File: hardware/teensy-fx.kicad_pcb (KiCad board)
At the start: 2 copper layers, 60 x 105 mm, 62 parts, among them J1 AudioJack3_Ground, J2 AudioJack3_Ground, SW1 Switch_SW_Push, SW2 Switch_SW_Push, SW3 Switch_SW_Push, SW4 Switch_SW_Push, U1 Teensy4.0, U2 AP7313-1.8V, U3 SGTL5000, U4 4067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

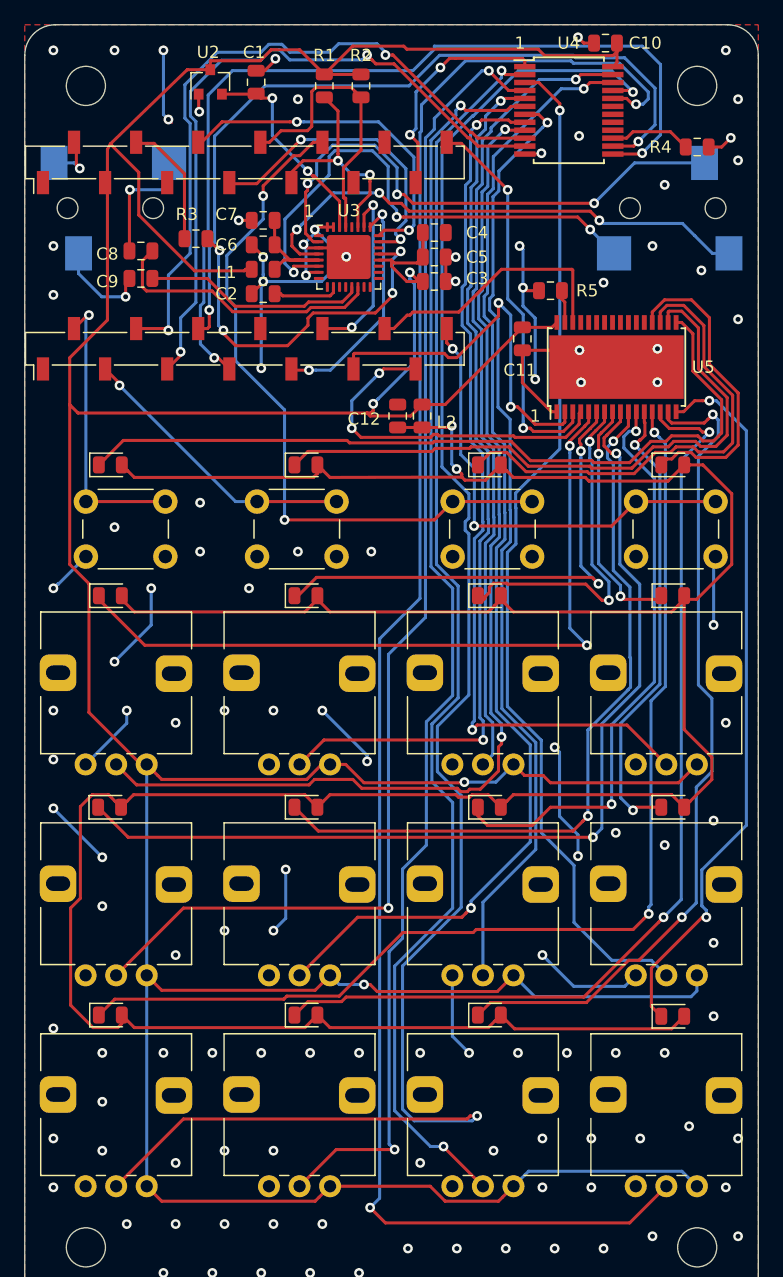
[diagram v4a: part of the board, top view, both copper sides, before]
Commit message: try to fix the wiring a bit, signal integrity might be an issue with 2 layer and teensy breakout
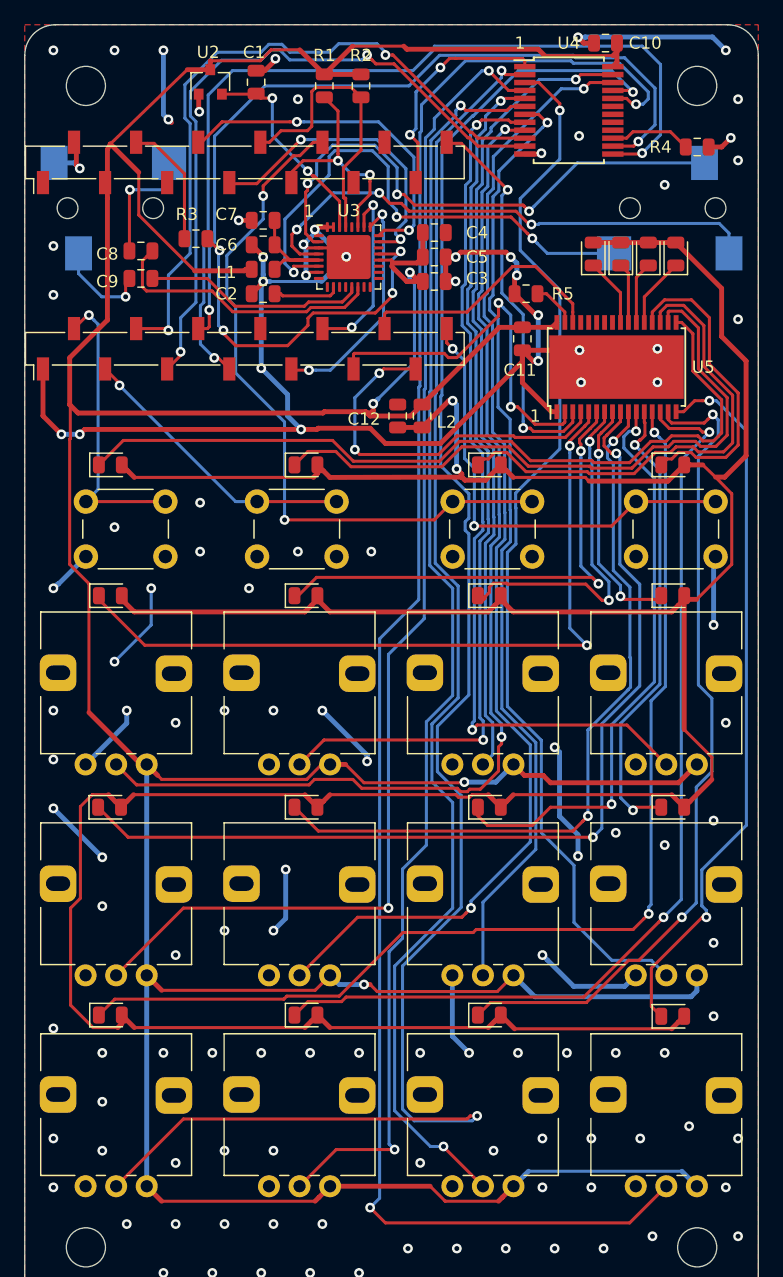
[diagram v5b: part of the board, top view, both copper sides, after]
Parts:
- added D17: LED, LED_SMD:LED_0805_2012Metric, F.Cu at (278.2, 63.8)
- added D18: LED, LED_SMD:LED_0805_2012Metric, F.Cu at (276.0, 63.8)
- added D19: LED, LED_SMD:LED_0805_2012Metric, F.Cu at (273.8, 63.8)
- added D20: LED, LED_SMD:LED_0805_2012Metric, F.Cu at (271.5, 63.8)
- moved R5 2.02 mm to (266.0, 67.0)
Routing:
- net GND: track 147.7 -> 218.1 mm, vias 122 -> 123
- net +3.3VA: track 265.4 -> 298.2 mm
- net Net-(D17-Pad1): track 0.00 -> 5.73 mm
- net Net-(D20-Pad1): track 0.00 -> 5.58 mm
- net Net-(D18-Pad1): track 0.00 -> 5.07 mm
- net Net-(D19-Pad1): track 0.00 -> 4.92 mm
- net /pots buttons & LEDs/a6: track 83.9 -> 86.6 mm
- net led_data: track 29.2 -> 30.9 mm
- net Net-(D13-Pad1): track 64.8 -> 66.1 mm
- net Net-(D14-Pad1): track 51.9 -> 52.9 mm
- net Net-(J2-PadS): track 42.6 -> 43.7 mm
- net led_latch: track 21.7 -> 21.0 mm
- net sw_1: track 23.5 -> 24.2 mm
- net Net-(R5-Pad1): track 3.15 -> 3.71 mm
- net Net-(J2-PadR): track 44.6 -> 45.2 mm
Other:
- net class power added: clearance 0.2, trace_width 0.4, via_dia 0.8, via_drill 0.4

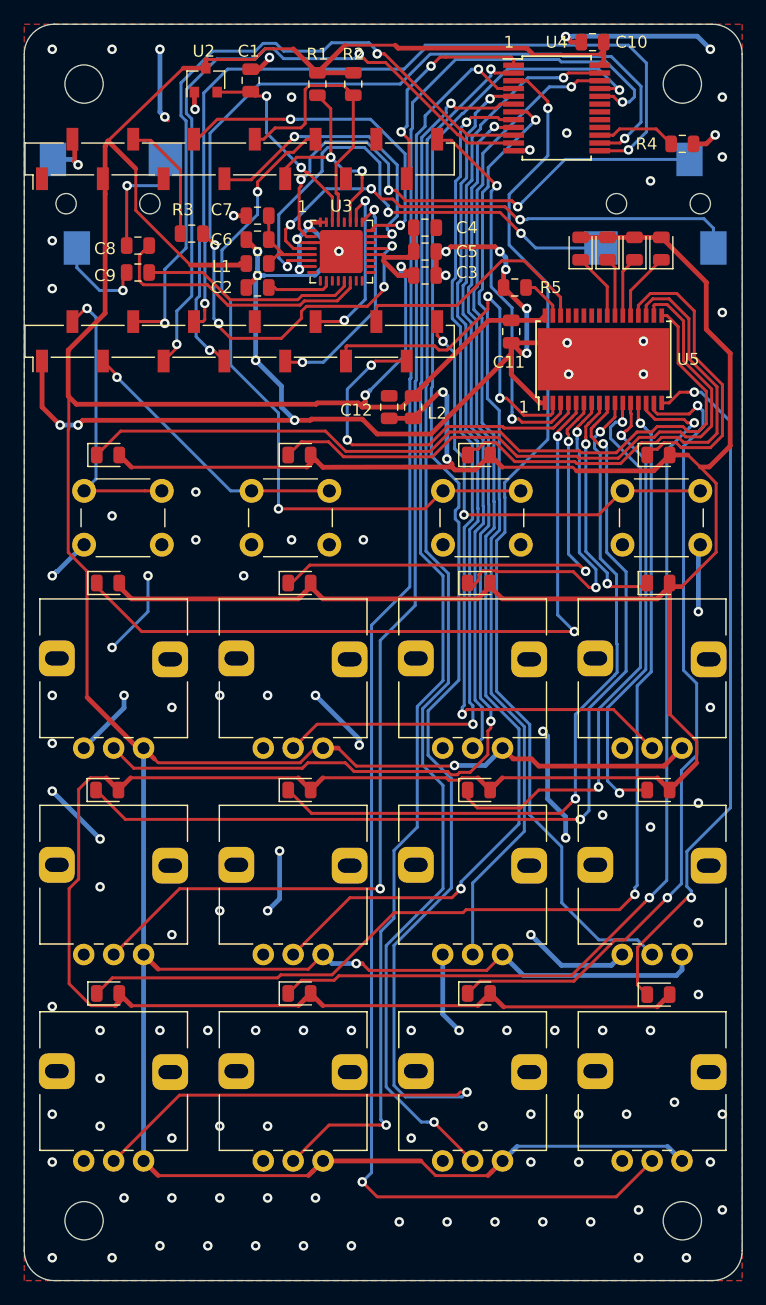
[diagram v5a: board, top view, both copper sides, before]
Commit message: move to 4 layer board, change size for cost, add optional flash
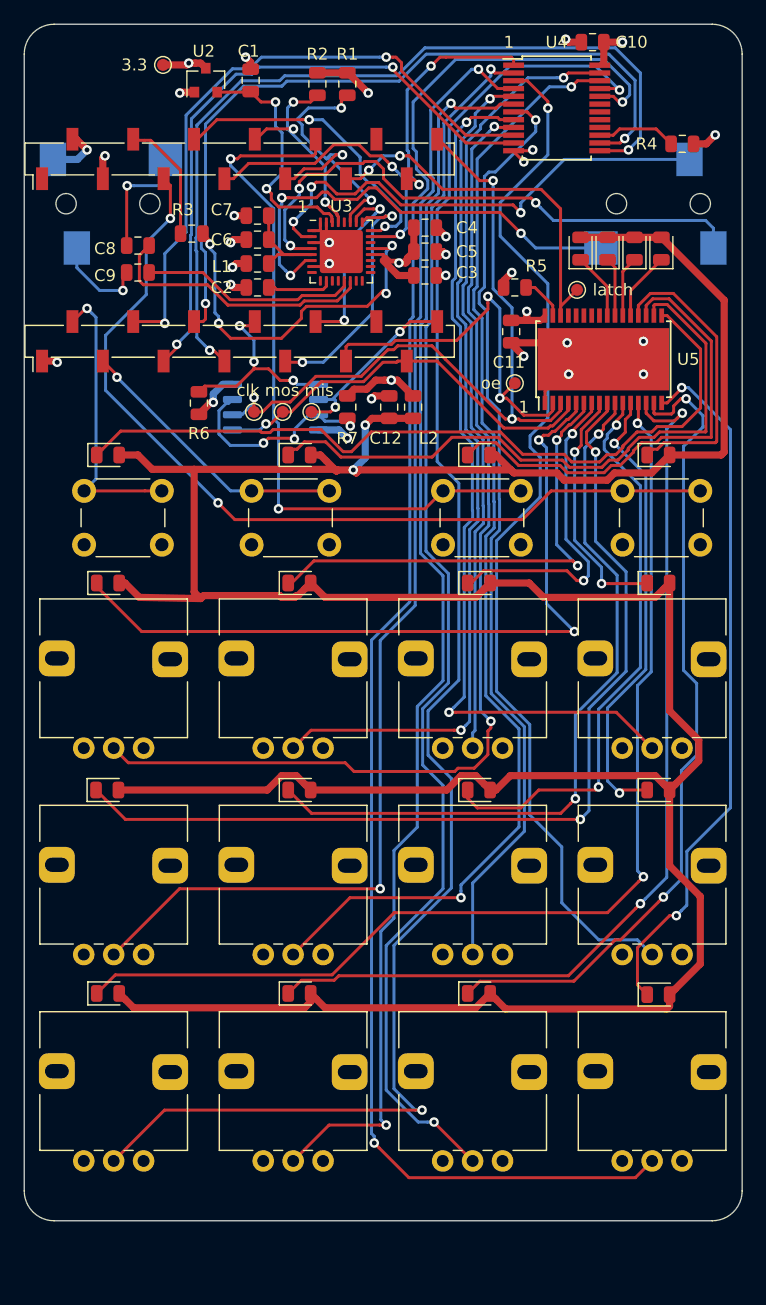
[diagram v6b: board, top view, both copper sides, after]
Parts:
- removed H1, H2, H3, H4: MountingHole, MountingHole:MountingHole_3.2mm_M3
- added R6: 10k, Resistor_SMD:R_0805_2012Metric, F.Cu at (239.6, 76.7)
- added R7: 10k, Resistor_SMD:R_0805_2012Metric, F.Cu at (252.0, 77.0)
- added TP1: TestPoint, TestPoint:TestPoint_Pad_D1.0mm, F.Cu at (244.2, 77.4)
- added TP2: TestPoint, TestPoint:TestPoint_Pad_D1.0mm, F.Cu at (266.0, 75.0)
- added TP3: TestPoint, TestPoint:TestPoint_Pad_D1.0mm, F.Cu at (246.6, 77.4)
- added TP4: TestPoint, TestPoint:TestPoint_Pad_D1.0mm, F.Cu at (271.2, 67.2)
- added TP5: TestPoint, TestPoint:TestPoint_Pad_D1.0mm, F.Cu at (249.0, 77.4)
- added TP6: TestPoint, TestPoint:TestPoint_Pad_D1.0mm, F.Cu at (236.6, 48.4)
- added U6: W25Q128JVS, Package_SO:SOIC-8_5.23x5.23mm_P1.27mm, B.Cu at (246.0, 77.0)
- moved R2 3.00 mm to (249.5, 50.0)
- moved R1 2.50 mm to (252.0, 50.0)
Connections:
- net led_clk renamed SCLK
- net led_data renamed MOSI
- U1 pad 12: led_latch -> Net-(U1-Pad12)
- U1 pad 14: sw_4 -> MISO
- U1 pad 23: Net-(U1-Pad23) -> led_latch
- U1 pad 29: Net-(U1-Pad29) -> sw_4
- U1 pad 8: Net-(U1-Pad8) -> /mem_cs
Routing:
- net +3V3: track 374.3 -> 41.0 mm, vias 4 -> 9
- net GND: track 218.1 -> 60.9 mm, vias 123 -> 24
- net sw_4: track 37.7 -> 75.3 mm
- net SCLK: track 32.1 -> 61.8 mm, vias 2 -> 3
- net Net-(R7-Pad2): track 0.00 -> 17.6 mm, vias 0 -> 3
- net /mem_cs: track 0.00 -> 16.8 mm, vias 0 -> 3
- net MISO: track 0.00 -> 15.6 mm, vias 0 -> 2
- net led_latch: track 21.0 -> 31.6 mm, vias 0 -> 2
- net /pots buttons & LEDs/a10: track 143.0 -> 134.9 mm
- net (no net): track 7.24 -> 0.00 mm, vias 2 -> 0
- net +3.3VA: track 298.2 -> 291.2 mm
- net SDA: track 18.5 -> 24.8 mm, vias 2 -> 3
- net SCL: track 23.5 -> 18.5 mm, vias 0 -> 3
- net /pots buttons & LEDs/a11: track 142.9 -> 138.8 mm
- net Net-(J2-PadS): track 43.7 -> 47.7 mm
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- added copper zone on In2.Cu, net +3V3
- added copper zone on In1.Cu, net GND
- removed copper zone on F.Cu, net GND
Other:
- board size 60 x 105 mm -> 60 x 100 mm
- copper layers 2 -> 4
- net class power: trace_width 0.4 -> 0.6
- board text added: "3.3"
- board text added: "clk mos mis"
- board text added: "latch"
- board text added: "oe"

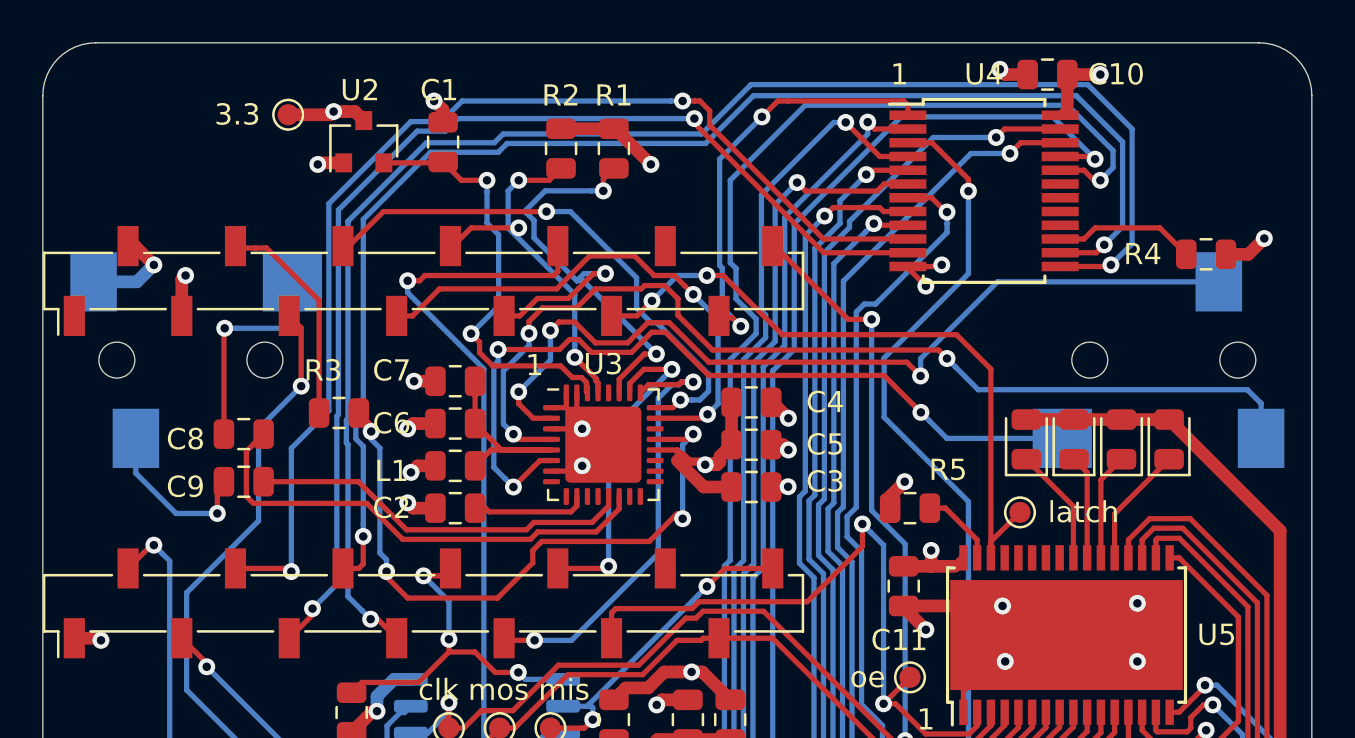
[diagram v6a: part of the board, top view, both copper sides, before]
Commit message: moved sockets in 2mm
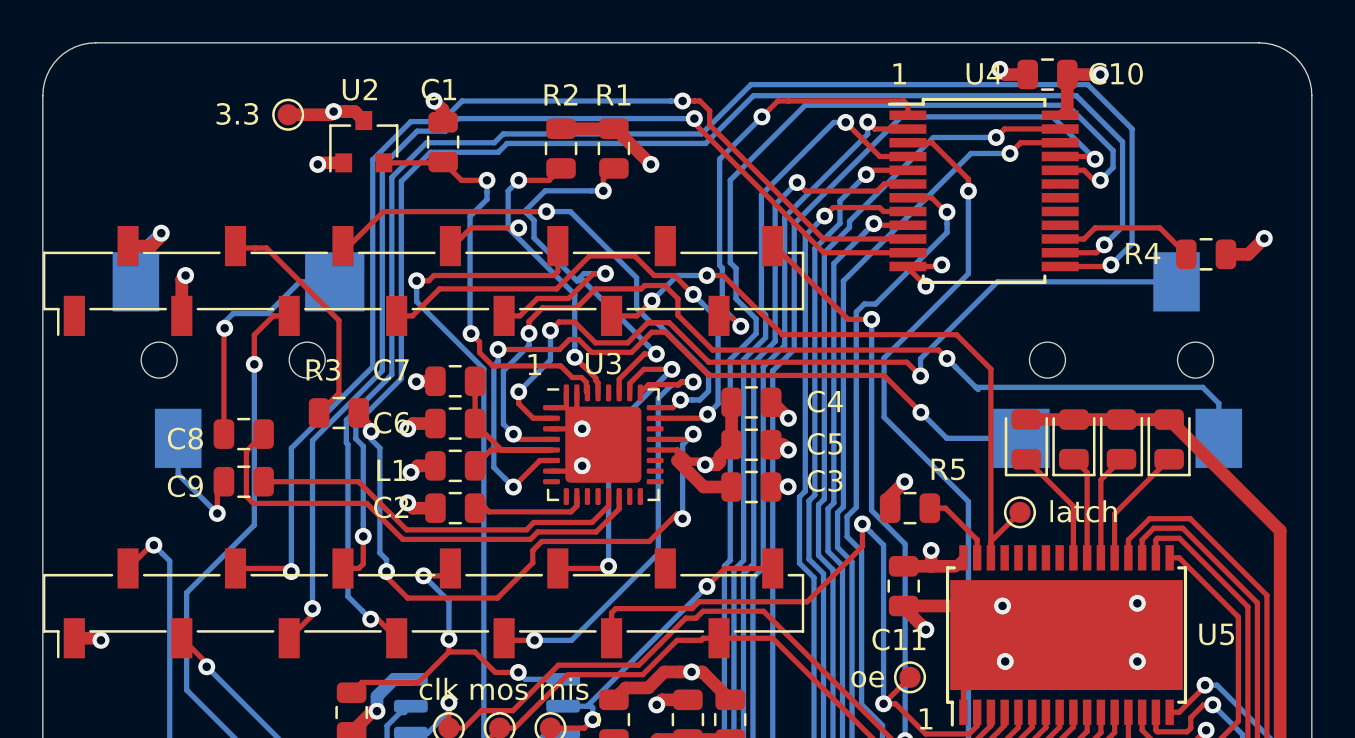
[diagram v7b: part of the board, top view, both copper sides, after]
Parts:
- moved J1 2.00 mm to (233.0, 60.0)
- moved J2 2.00 mm to (277.0, 60.0)
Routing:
- net Net-(J2-PadT): track 38.9 -> 36.9 mm
- net Net-(J2-PadR): track 41.9 -> 39.9 mm
- net Net-(C9-Pad2): track 7.92 -> 5.95 mm
- net Net-(J2-PadS): track 47.7 -> 45.8 mm
- net Net-(C8-Pad2): track 10.1 -> 11.3 mm
- net MCLK: track 10.1 -> 10.9 mm
- net sw_3: track 60.3 -> 59.7 mm

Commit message: fix sgtl5000 symbol error, add filter resistor and cap for unused mic input
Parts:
- added C13: 0.1uF, Capacitor_SMD:C_0805_2012Metric, F.Cu at (221.0, 79.2)
- added R8: 1k, Resistor_SMD:R_0805_2012Metric, F.Cu at (220.6, 75.4)
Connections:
- C3 pad 1: +3V3 -> Net-(C3-Pad1)
- C4 pad 1: +3V3 -> Net-(C3-Pad1)
- C5 pad 1: +3V3 -> Net-(C3-Pad1)
- L1 pad 1: +3V3 -> Net-(C3-Pad1)
- U1 pad 10: TX -> I2S_IN
- U1 pad 9: RX -> I2S_OUT
- U3 pad 20: +3V3 -> Net-(C3-Pad1)
- U3 pad 25: RX -> I2S_IN
- U3 pad 26: TX -> I2S_OUT
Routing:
- net Net-(C3-Pad1): track 0.00 -> 12.1 mm, vias 0 -> 2
- net +3V3: track 41.0 -> 29.0 mm, vias 9 -> 7
